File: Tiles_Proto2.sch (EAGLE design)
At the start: 47 parts, among them J1 7p-SMD-2.54, Q1 MMBT3904LT1G, U1 ADXL345BCCZ-RL, U2 MPR121QR2, U3 MCP73832T-2ACI/OT-SOT23-5

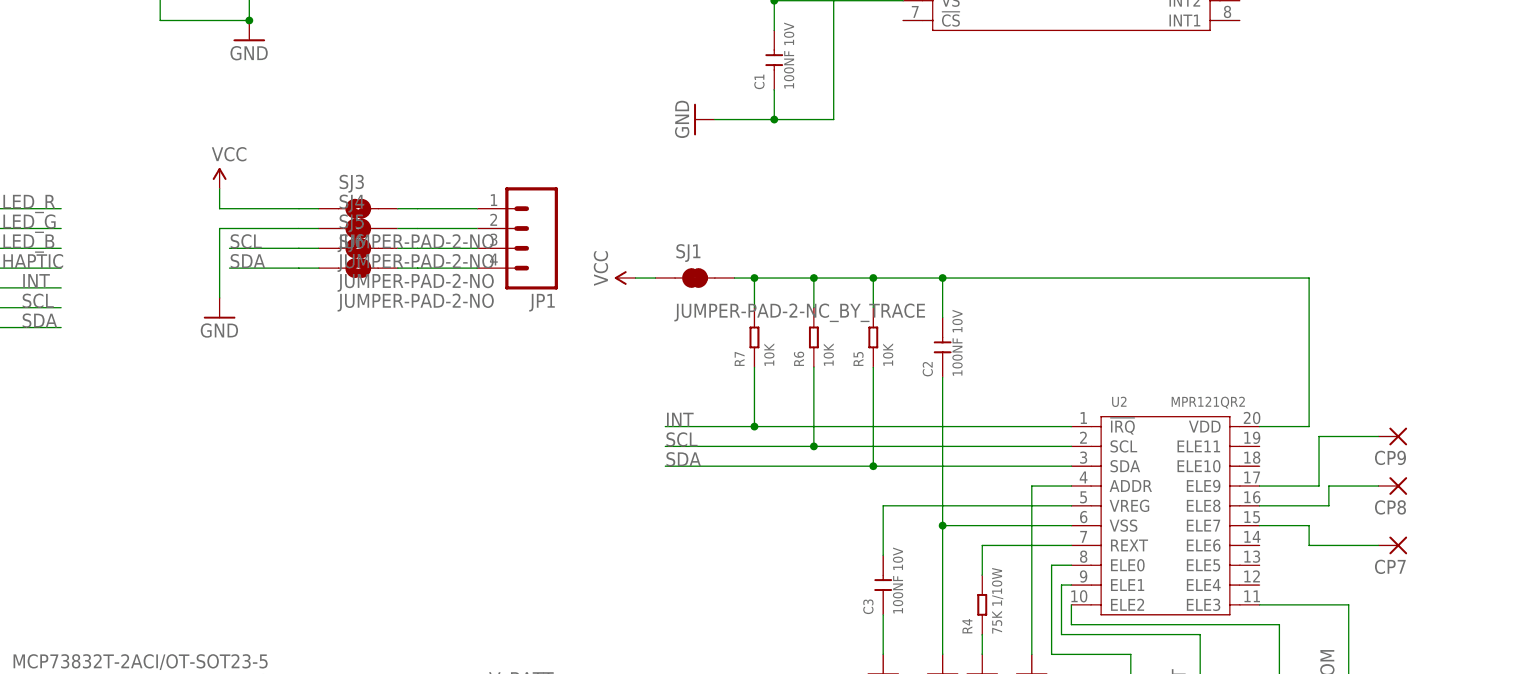
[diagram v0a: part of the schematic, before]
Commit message: fixed 6 pins header
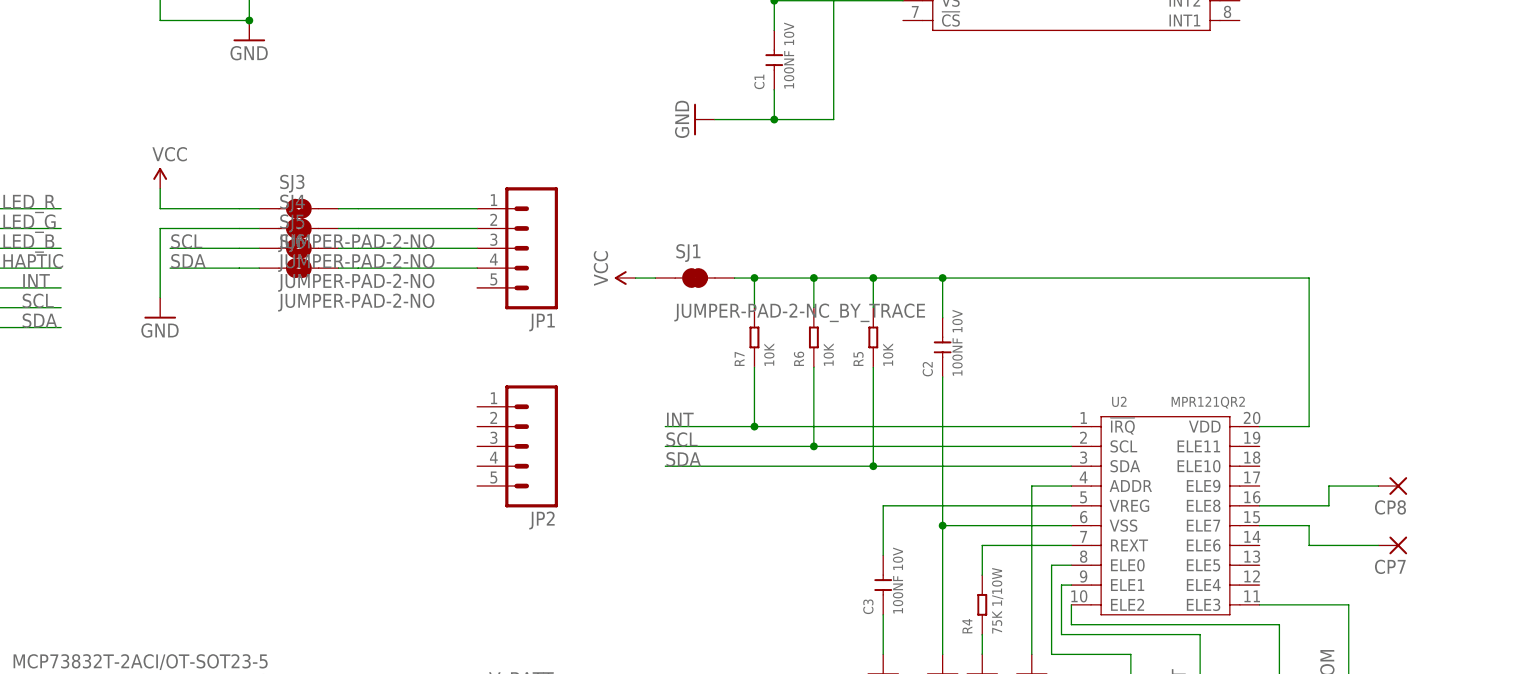
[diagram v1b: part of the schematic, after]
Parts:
- removed CP9: (no value), wirepad:SMD2
- added JP2: (no value), SparkFun-Connectors:M05PTH
- JP1: device SparkFun-Connectors:M04PTH -> SparkFun-Connectors:M05PTH
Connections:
- removed net N$22: CP9.P, U2.ELE9
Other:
- moved on the sheet: SJ3, SJ4, SJ5, SJ6
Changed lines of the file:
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@@
 <part name="GND15" library="SparkFun-Aesthetics" deviceset="GND" device=""/>
 <part name="GND16" library="SparkFun-Aesthetics" deviceset="GND" device=""/>
-<part name="JP1" library="SparkFun-Connectors" deviceset="M04" device="PTH"/>
+<part name="JP1" library="SparkFun-Connectors" deviceset="M05" device="PTH"/>
 <part name="SUPPLY8" library="SparkFun-Aesthetics" deviceset="VCC" device=""/>
 <part name="GND17" library="SparkFun-Aesthetics" deviceset="GND" device=""/>
@@
 <part name="CP7" library="wirepad" deviceset="SMD2" device=""/>
 <part name="CP8" library="wirepad" deviceset="SMD2" device=""/>
-<part name="CP9" library="wirepad" deviceset="SMD2" device=""/>
 <part name="SJ1" library="SparkFun-Passives" deviceset="JUMPER-PAD-2-NC_BY_TRACE" device=""/>
 <part name="SJ2" library="SparkFun-Passives" deviceset="JUMPER-PAD-2-NC_BY_TRACE" device=""/>
@@
 <part name="SJ6" library="SparkFun-Passives" deviceset="JUMPER-PAD-2-NO" device=""/>
 <part name="USB1" library="Seeed-OPL-Connector" deviceset="MICRO-USB-SMD-B-(10118193-0001LF)" device="" value="10118193-0001LF"/>
+<part name="JP2" library="SparkFun-Connectors" deviceset="M05" device="PTH"/>
 </parts>
 <sheets>
@@
 <instance part="GND15" gate="1" x="13.97" y="86.36" rot="R270"/>
 <instance part="GND16" gate="1" x="50.8" y="58.42"/>
-<instance part="JP1" gate="G$1" x="142.24" y="99.06" rot="R180"/>
-<instance part="SUPPLY8" gate="G$1" x="104.14" y="104.14"/>
-<instance part="GND17" gate="1" x="104.14" y="87.63"/>
+<instance part="JP1" gate="G$1" x="144.78" y="96.52" rot="R180"/>
+<instance part="SUPPLY8" gate="G$1" x="96.52" y="104.14"/>
+<instance part="GND17" gate="1" x="96.52" y="87.63"/>
 <instance part="R11" gate="G$1" x="241.3" y="149.86" rot="R90"/>
 <instance part="R12" gate="G$1" x="251.46" y="149.86" rot="R90"/>
@@
 <instance part="CP7" gate="1" x="255.27" y="58.42" rot="R180"/>
 <instance part="CP8" gate="1" x="255.27" y="66.04" rot="R180"/>
-<instance part="CP9" gate="1" x="255.27" y="72.39" rot="R180"/>
 <instance part="SJ1" gate="G$1" x="165.1" y="92.71"/>
 <instance part="SJ2" gate="G$1" x="175.26" y="149.86" rot="R90"/>
-<instance part="SJ3" gate="G$1" x="121.92" y="101.6"/>
-<instance part="SJ4" gate="G$1" x="121.92" y="99.06"/>
-<instance part="SJ5" gate="G$1" x="121.92" y="96.52"/>
-<instance part="SJ6" gate="G$1" x="121.92" y="93.98"/>
+<instance part="SJ3" gate="G$1" x="114.3" y="101.6"/>
+<instance part="SJ4" gate="G$1" x="114.3" y="99.06"/>
+<instance part="SJ5" gate="G$1" x="114.3" y="96.52"/>
+<instance part="SJ6" gate="G$1" x="114.3" y="93.98"/>
 <instance part="USB1" gate="G$1" x="20.32" y="30.48"/>
+<instance part="JP2" gate="G$1" x="144.78" y="71.12" rot="R180"/>
 </instances>
 <busses>
@@
 </segment>
 <segment>
-<wire x1="105.41" y1="96.52" x2="114.3" y2="96.52" width="0.1524" layer="91"/>
-<label x="105.41" y="96.52" size="1.778" layer="95"/>
+<wire x1="97.79" y1="96.52" x2="106.68" y2="96.52" width="0.1524" layer="91"/>
+<label x="97.79" y="96.52" size="1.778" layer="95"/>
 <pinref part="SJ5" gate="G$1" pin="1"/>
-<wire x1="114.3" y1="96.52" x2="116.84" y2="96.52" width="0.1524" layer="91"/>
+<wire x1="106.68" y1="96.52" x2="109.22" y2="96.52" width="0.1524" layer="91"/>
 </segment>
 </net>
@@
 </segment>
 <segment>
-<wire x1="105.41" y1="93.98" x2="114.3" y2="93.98" width="0.1524" layer="91"/>
-<label x="105.41" y="93.98" size="1.778" layer="95"/>
+<wire x1="97.79" y1="93.98" x2="106.68" y2="93.98" width="0.1524" layer="91"/>
+<label x="97.79" y="93.98" size="1.778" layer="95"/>
 <pinref part="SJ6" gate="G$1" pin="1"/>
-<wire x1="114.3" y1="93.98" x2="116.84" y2="93.98" width="0.1524" layer="91"/>
+<wire x1="106.68" y1="93.98" x2="109.22" y2="93.98" width="0.1524" layer="91"/>
 </segment>
 </net>
@@
 <segment>
 <pinref part="GND17" gate="1" pin="GND"/>
-<wire x1="104.14" y1="90.17" x2="104.14" y2="99.06" width="0.1524" layer="91"/>
-<wire x1="104.14" y1="99.06" x2="114.3" y2="99.06" width="0.1524" layer="91"/>
+<wire x1="96.52" y1="90.17" x2="96.52" y2="99.06" width="0.1524" layer="91"/>
+<wire x1="96.52" y1="99.06" x2="106.68" y2="99.06" width="0.1524" layer="91"/>
 <pinref part="SJ4" gate="G$1" pin="1"/>
-<wire x1="114.3" y1="99.06" x2="116.84" y2="99.06" width="0.1524" layer="91"/>
+<wire x1="106.68" y1="99.06" x2="109.22" y2="99.06" width="0.1524" layer="91"/>
 </segment>
 <segment>
@@
 <segment>
 <pinref part="SUPPLY8" gate="G$1" pin="VCC"/>
-<wire x1="104.14" y1="104.14" x2="104.14" y2="101.6" width="0.1524" layer="91"/>
-<wire x1="104.14" y1="101.6" x2="114.3" y2="101.6" width="0.1524" layer="91"/>
+<wire x1="96.52" y1="104.14" x2="96.52" y2="101.6" width="0.1524" layer="91"/>
+<wire x1="96.52" y1="101.6" x2="106.68" y2="101.6" width="0.1524" layer="91"/>
 <pinref part="SJ3" gate="G$1" pin="1"/>
-<wire x1="114.3" y1="101.6" x2="116.84" y2="101.6" width="0.1524" layer="91"/>
+<wire x1="106.68" y1="101.6" x2="109.22" y2="101.6" width="0.1524" layer="91"/>
 </segment>
 <segment>
@@
 <segment>
 <pinref part="JP1" gate="G$1" pin="1"/>
-<wire x1="129.54" y1="101.6" x2="137.16" y2="101.6" width="0.1524" layer="91"/>
+<wire x1="121.92" y1="101.6" x2="137.16" y2="101.6" width="0.1524" layer="91"/>
 <pinref part="SJ3" gate="G$1" pin="2"/>
-<wire x1="127" y1="101.6" x2="129.54" y2="101.6" width="0.1524" layer="91"/>
+<wire x1="119.38" y1="101.6" x2="121.92" y2="101.6" width="0.1524" layer="91"/>
 </segment>
 </net>
@@
 <segment>
 <pinref part="JP1" gate="G$1" pin="2"/>
-<wire x1="129.54" y1="99.06" x2="137.16" y2="99.06" width="0.1524" layer="91"/>
+<wire x1="121.92" y1="99.06" x2="137.16" y2="99.06" width="0.1524" layer="91"/>
 <pinref part="SJ4" gate="G$1" pin="2"/>
-<wire x1="127" y1="99.06" x2="129.54" y2="99.06" width="0.1524" layer="91"/>
+<wire x1="119.38" y1="99.06" x2="121.92" y2="99.06" width="0.1524" layer="91"/>
 </segment>
 </net>
@@
 <segment>
 <pinref part="JP1" gate="G$1" pin="3"/>
-<wire x1="129.54" y1="96.52" x2="137.16" y2="96.52" width="0.1524" layer="91"/>
+<wire x1="121.92" y1="96.52" x2="137.16" y2="96.52" width="0.1524" layer="91"/>
 <pinref part="SJ5" gate="G$1" pin="2"/>
-<wire x1="127" y1="96.52" x2="129.54" y2="96.52" width="0.1524" layer="91"/>
+<wire x1="119.38" y1="96.52" x2="121.92" y2="96.52" width="0.1524" layer="91"/>
 </segment>
 </net>
@@
 <segment>
 <pinref part="JP1" gate="G$1" pin="4"/>
-<wire x1="129.54" y1="93.98" x2="137.16" y2="93.98" width="0.1524" layer="91"/>
+<wire x1="121.92" y1="93.98" x2="137.16" y2="93.98" width="0.1524" layer="91"/>
 <pinref part="SJ6" gate="G$1" pin="2"/>
-<wire x1="127" y1="93.98" x2="129.54" y2="93.98" width="0.1524" layer="91"/>
+<wire x1="119.38" y1="93.98" x2="121.92" y2="93.98" width="0.1524" layer="91"/>
 </segment>
 </net>
@@
 </segment>
 </net>
-<net name="N$22" class="0">
-<segment>
-<pinref part="U2" gate="G$1" pin="ELE9"/>
-<wire x1="237.49" y1="66.04" x2="245.11" y2="66.04" width="0.1524" layer="91"/>
-<wire x1="245.11" y1="66.04" x2="245.11" y2="72.39" width="0.1524" layer="91"/>
-<pinref part="CP9" gate="1" pin="P"/>
-<wire x1="245.11" y1="72.39" x2="252.73" y2="72.39" width="0.1524" layer="91"/>
-</segment>
-</net>
